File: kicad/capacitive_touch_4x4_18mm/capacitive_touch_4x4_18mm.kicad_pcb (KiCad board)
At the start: 2 copper layers, 20.6 x 18.5 mm, 2 parts, among them J4 Capacitive_touch_grid_4x4, J6 Conn_01x08

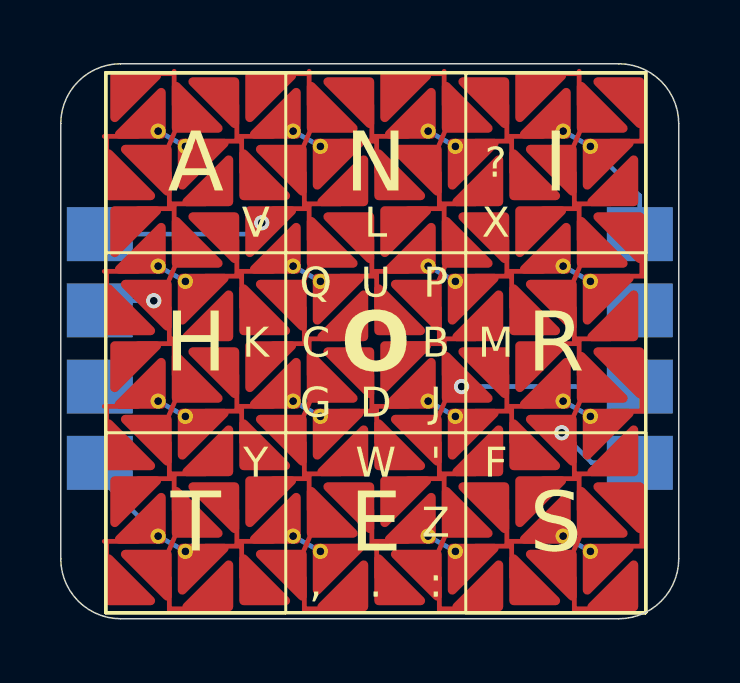
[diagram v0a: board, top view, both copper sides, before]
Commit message: Add a larger touch pad & modify design for jlcpcb
- Create new 50mm touch pad design with 6x6 grid
- Modify design to be suitable for jlcpcb
- Update scripts to generate new 6x6 design outputs
- Add silkscreen script to produce silkscreen SVGs for keyboard
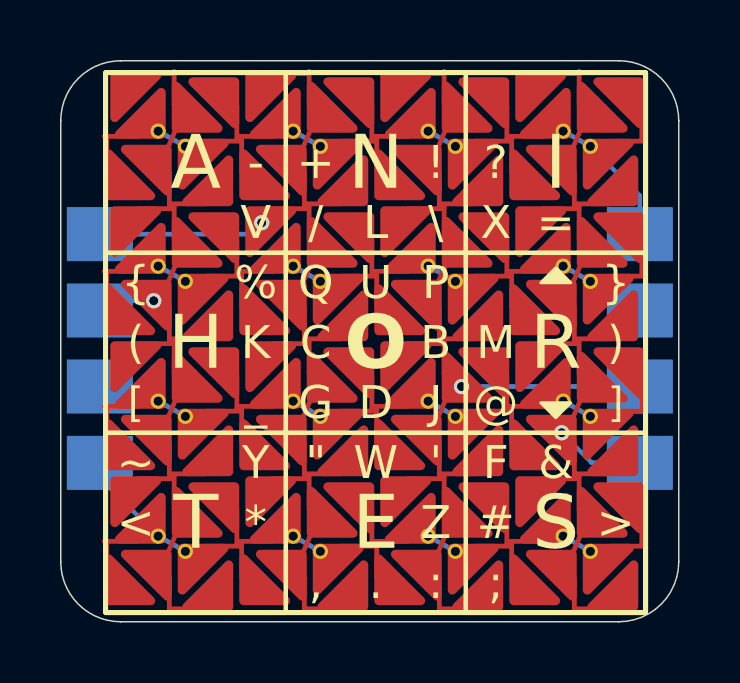
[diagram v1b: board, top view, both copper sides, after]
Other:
- board size 20.6 x 18.5 mm -> 20.6 x 18.7 mm
- board text added: "!"
- board text added: "#"
- board text added: "%"
- board text added: "&"
- board text added: "("
- board text added: ")"
- board text added: "*"
- board text added: "+"
- board text added: "-"
- board text added: "/"
- board text added: ";"
- board text added: "<"
- board text added: "="
- board text added: ">"
- board text added: "@"
- board text added: "["
- board text added: "\"
- board text added: "]"
- board text added: "_"
- board text added: "{"
- board text added: "{dblquote}"
- board text added: "}"
- board text added: "~"

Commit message: Add generated build files and final changes
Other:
- board text added: "Designed by: Luke Thompson Illumneo"
- board text added: "github.com/ illumneo/capkey"
- board text added: "supercon2025"
- board text removed: "Capacitive Touch Keycap"
- board text removed: "Luke Thompson 2025-06-12"
